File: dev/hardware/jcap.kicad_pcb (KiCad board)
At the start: 2 copper layers, 133 x 87 mm, 63 parts, among them J201 CPU PGMR, J202 SPARE CPU HDR, J203 GPU PGMR, J204 SPARE GPU HDR, J301 DC IN, J501 VGA OUT, J601 CONTROLS, SW201 CPU ~{RES}, SW202 DEBUG, SW203 GPU ~{RES}, SW601 TILT, U201 P8X32A-D40, U202 P8X32A-D40, U301 LF33_TO220, U401 24LC256, U402 24LC256, U601 74HC165, U602 74HC165, Y201 6.5MHz, Y202 6.5MHz

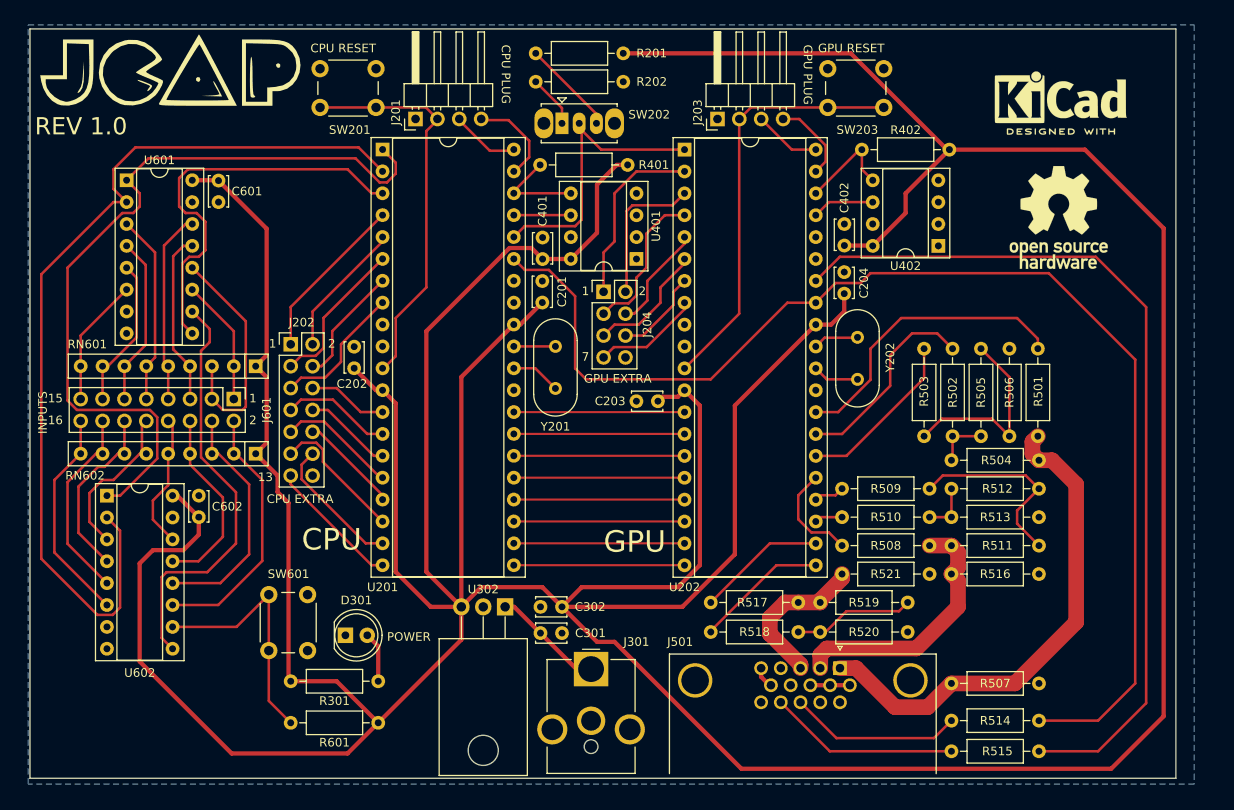
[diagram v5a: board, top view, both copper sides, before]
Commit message: Implemented review changes - missing reverse polarity protection
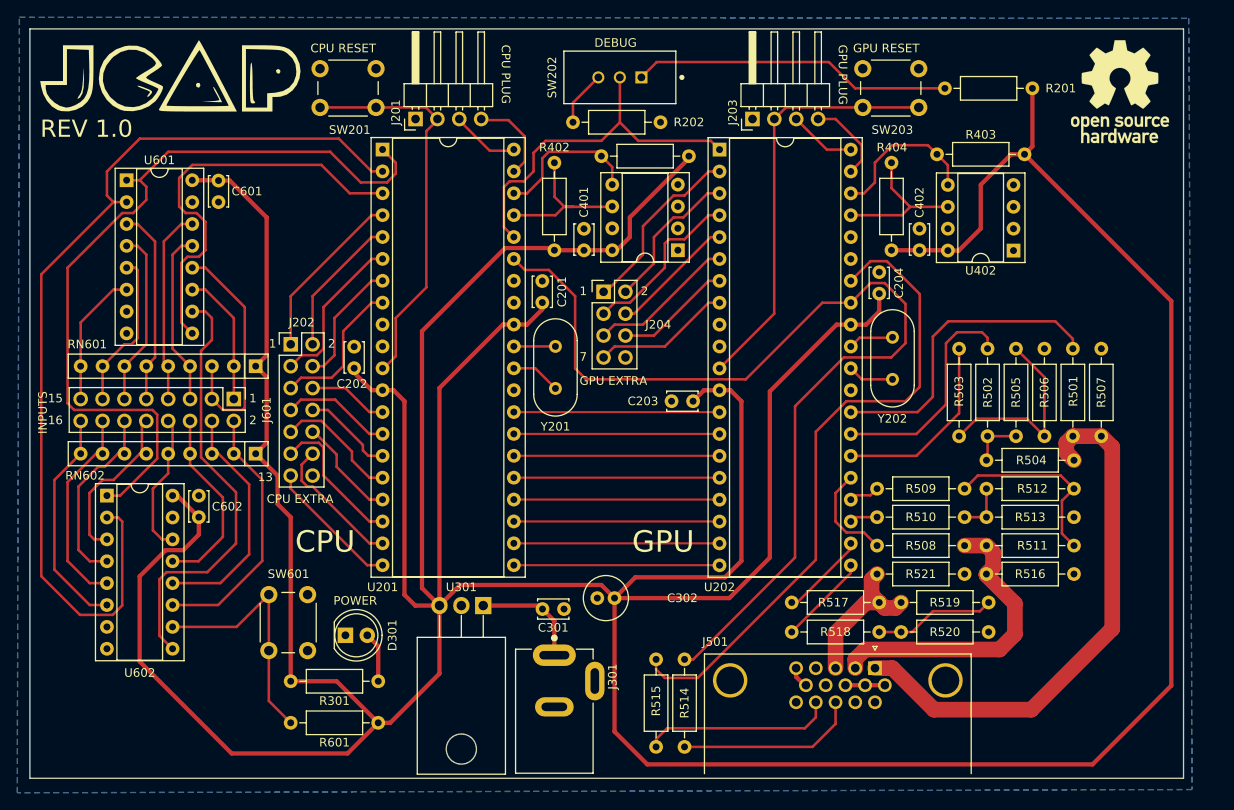
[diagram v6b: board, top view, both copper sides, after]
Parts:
- removed the REF** at (217.7, 73.9)
- added R402: 4.7K, Resistor_THT:R_Axial_DIN0207_L6.3mm_D2.5mm_P10.16mm_Horizontal, F.Cu at (158.9, 81.5)
- added R404: 4.7K, Resistor_THT:R_Axial_DIN0207_L6.3mm_D2.5mm_P10.16mm_Horizontal, F.Cu at (198.0, 81.5)
- C301: value 0.1u -> .47u
- C302: value 10u -> 47u; footprint Capacitor_THT:C_Disc_D3.4mm_W2.1mm_P2.50mm -> Capacitor_THT:C_Radial_D5.0mm_H11.0mm_P2.00mm
- G***: footprint LOGO -> jcap-footprints:LOGO
- J301: footprint Connector_BarrelJack:BarrelJack_CUI_PJ-063AH_Horizontal_CircularHoles -> jcap-footprints:CUI_PJ-202AH
- R401: value 10K -> 4.7K
- R403: renamed from R402; value 10K -> 4.7K
- SW202: footprint Button_Switch_THT:SW_Slide_1P2T_CK_OS102011MS2Q -> jcap-footprints:SW_1825159-1
- U301: footprint Package_TO_SOT_THT:TO-220-3_Horizontal_TabDown -> jcap-footprints:TO-220-3_Horizontal_TabDown
- moved R201 47.7 mm to (204.2, 72.9)
- moved R514 41.8 mm to (174.0, 139.2), turned to -90 degrees
- moved R507 39.5 mm to (222.4, 103.1), turned to -90 degrees
- moved R515 34.3 mm to (170.7, 149.4), turned to 90 degrees
- moved REF** 16.2 mm to (224.5, 73.3)
- moved R517 9.40 mm to (196.6, 132.6)
- moved R518 9.40 mm to (196.6, 136.0)
- moved R519 9.40 mm to (199.1, 132.6)
- moved R520 9.40 mm to (199.1, 136.0)
- moved C402 8.74 mm to (201.3, 89.2)
- moved R403 8.74 mm to (203.3, 80.6)
- moved U402 8.74 mm to (212.2, 91.7)
- moved C302 8.66 mm to (165.9, 132.1), turned to 180 degrees
- moved SW202 8.58 mm to (166.5, 71.6), turned to 180 degrees
- moved R401 7.18 mm to (164.3, 80.8)
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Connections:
- C302 pad 1: GND -> +3.3V
- C302 pad 2: +3.3V -> GND
- R201 pad 1: Net-(SW202-C) -> Net-(R201-Pad1)
- R202 pad 2: Net-(SW202-A) -> Net-(R202-Pad2)
- SW202 pad 1: Net-(SW202-A) -> Net-(R201-Pad1)
- SW202 pad 3: Net-(SW202-C) -> Net-(R202-Pad2)
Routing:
- net Net-(R201-Pad1): track 0.00 -> 37.2 mm
- net +3.3V: track 642.8 -> 612.8 mm
- net H_SYNC: track 102.7 -> 76.2 mm
- net V_SYNC: track 142.7 -> 117.5 mm
- net SCL_CPU: track 6.62 -> 18.3 mm
- net Net-(SW202-C): track 11.0 -> 0.00 mm
- net SCL_GPU: track 7.24 -> 17.7 mm
- net /Propellers/DEBUG: track 33.8 -> 42.2 mm
- net SDA_GPU: track 11.5 -> 18.2 mm
- net Net-(R202-Pad2): track 0.00 -> 6.43 mm
- net SDA_CPU: track 11.2 -> 17.3 mm
- net Net-(SW202-A): track 6.09 -> 0.00 mm
- net /VGA_DAC/GREEN_OUT: track 30.4 -> 35.6 mm
- net BLUE1: track 15.0 -> 10.1 mm
- net BLUE2: track 15.5 -> 10.6 mm
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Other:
- board size 133 x 87 mm -> 133.9 x 87 mm
- board text added: "DEBUG"
- board text removed: "U302"

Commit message: Finalized physical layout
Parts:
- added Q301: IPP80P03P4L-04, Package_TO_SOT_THT:TO-220-3_Horizontal_TabDown, F.Cu at (134.9, 151.0)
- moved D301 47.4 mm to (180.6, 147.8), turned to 90 degrees
- moved R301 46.3 mm to (174.5, 139.2), turned to -90 degrees
- moved J501 17.8 mm to (213.9, 140.2)
- moved R514 17.5 mm to (191.5, 139.2)
- moved R515 17.3 mm to (188.0, 149.4)
- moved R601 14.9 mm to (118.4, 135.4), turned to -90 degrees
- moved C302 13.9 mm to (179.6, 134.4)
- moved R520 12.7 mm to (186.4, 136.0)
- moved R518 12.0 mm to (206.5, 129.3)
- moved R521 9.98 mm to (199.1, 136.0), turned to 0 degrees
- moved C301 8.99 mm to (156.3, 141.5), turned to 0 degrees
- moved J301 6.57 mm to (165.4, 145.0)
- moved SW601 4.23 mm to (128.3, 135.4)
- moved U301 1.11 mm to (151.6, 132.5)
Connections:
- C301 pad 2: Net-(U301-IN) -> Net-(Q301-S)
- J301 pad 1: Net-(U301-IN) -> Net-(Q301-S)
- U301 pad 1: Net-(U301-IN) -> Net-(Q301-D)
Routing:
- net Net-(Q301-S): track 0.00 -> 33.4 mm
- net +3.3V: track 612.8 -> 581.5 mm
- net Net-(Q301-D): track 0.00 -> 26.3 mm
- net /VGA_DAC/RED_OUT: track 63.1 -> 41.2 mm
- net /VGA_DAC/GREEN_OUT: track 35.6 -> 21.1 mm
- net Net-(R518-Pad1): track 14.1 -> 27.6 mm
- net Net-(U301-IN): track 13.0 -> 0.00 mm
- net Net-(U602-DS): track 28.7 -> 15.7 mm
- net H_SYNC: track 76.2 -> 65.9 mm
- net BLUE2: track 10.6 -> 3.47 mm
- net V_SYNC: track 117.5 -> 122.8 mm
- net Net-(D301-A): track 5.86 -> 8.53 mm
- net /VGA_DAC/BLUE_OUT: track 17.6 -> 18.8 mm
- net Net-(J501-Pad14): track 22.2 -> 22.9 mm
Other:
- board text added: "+5V DC"
- board text added: "GFX_DATA[0]"
- board text added: "GFX_DATA[1]"
- board text added: "GFX_DATA[2]"
- board text added: "GFX_DATA[3]"
- board text added: "GFX_DATA[4]"
- board text added: "GFX_DATA[5]"
- board text added: "GFX_DATA[6]"
- board text added: "GFX_DATA[7]"
- board text added: "TILT"

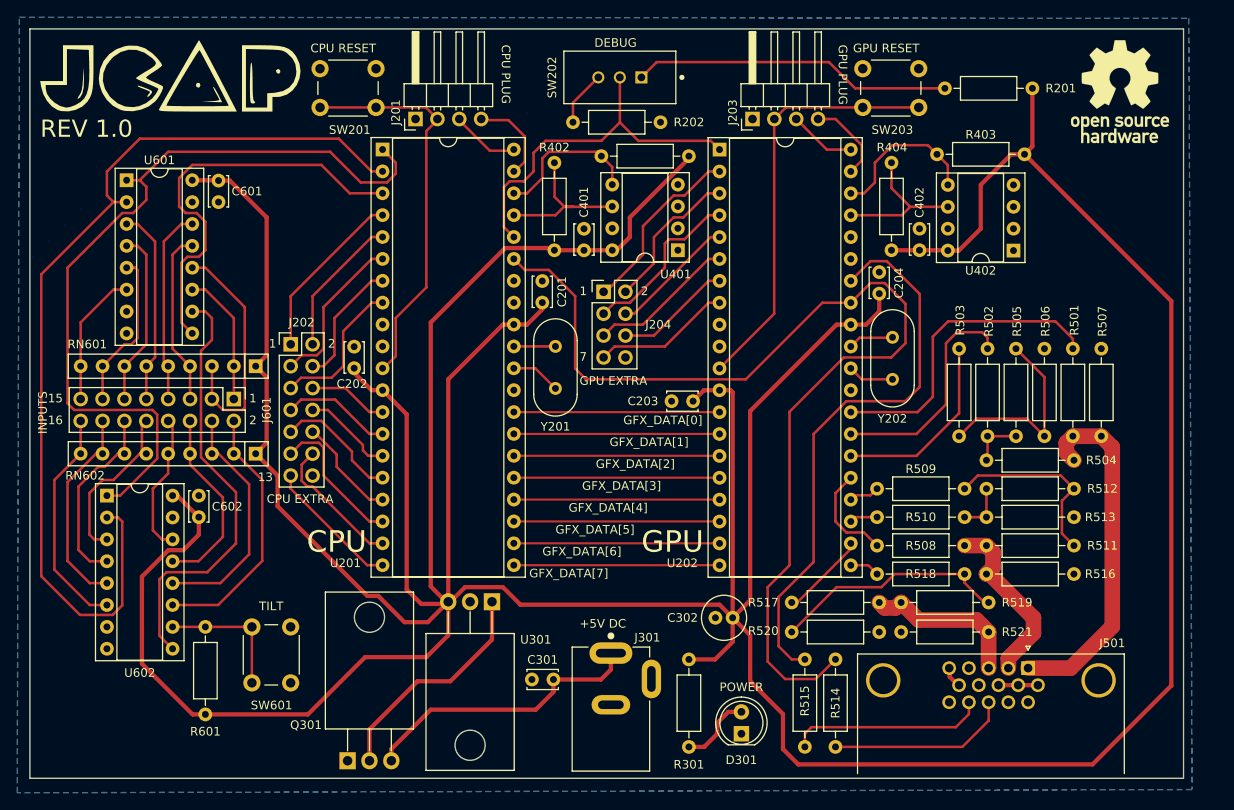
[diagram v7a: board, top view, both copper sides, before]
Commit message: Finalized dev PCB for 1st run
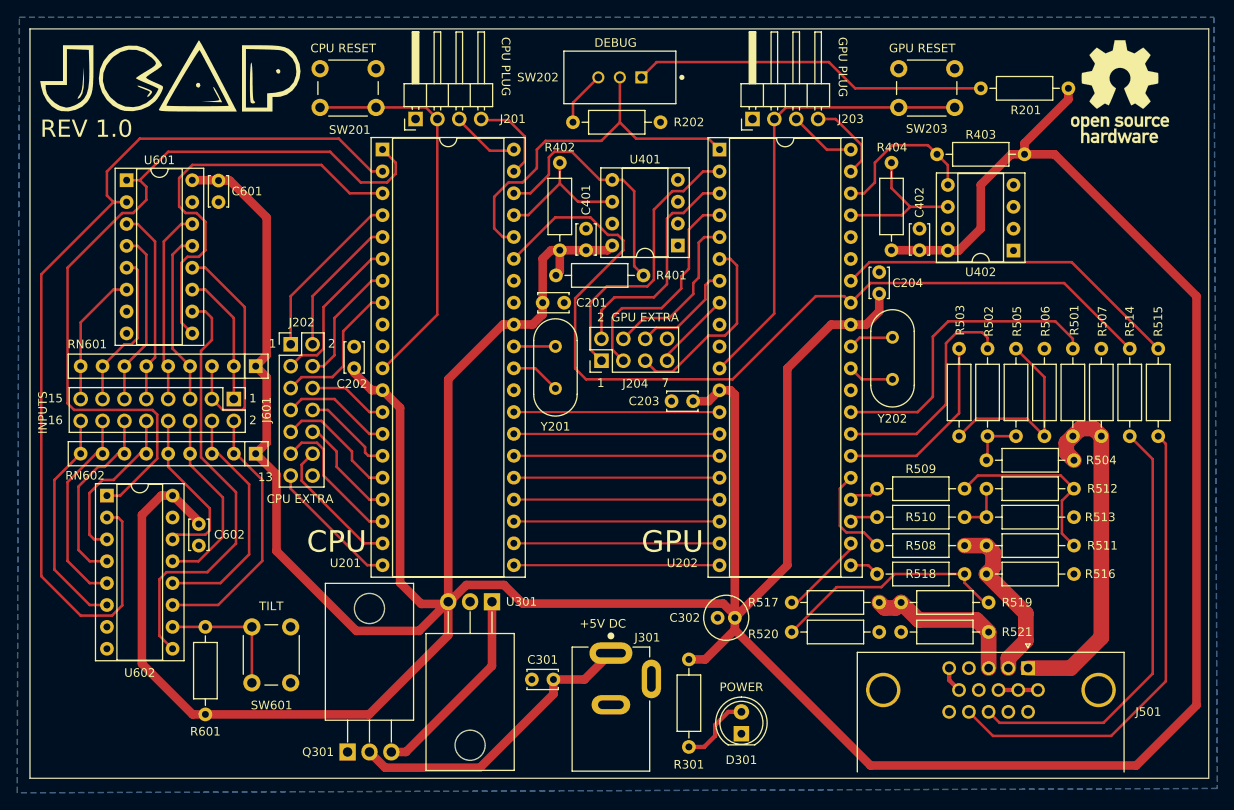
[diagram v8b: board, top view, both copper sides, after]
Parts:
- J501: footprint Connector_Dsub:DSUB-15-HD_Female_Horizontal_P2.29x1.98mm_EdgePinOffset8.35mm_Housed_MountingHolesOffset10.89mm -> jcap-footprints:2311763-2
- moved R515 54.6 mm to (229.0, 113.3)
- moved R514 49.7 mm to (225.7, 103.1)
- moved R401 14.7 mm to (169.2, 94.6), turned to 180 degrees
- moved J204 8.00 mm to (164.3, 104.5), turned to 90 degrees
- moved C602 5.80 mm to (117.6, 126.0), turned to 90 degrees
- moved SW203 4.18 mm to (198.9, 70.6)
- moved R201 4.18 mm to (208.4, 72.9)
- moved C201 3.58 mm to (160.0, 97.8), turned to 180 degrees
- moved Q301 1.02 mm to (134.9, 149.9)
- moved R402 0.63 mm to (159.5, 81.5)
- moved U401 0.55 mm to (173.2, 91.1)
- moved C302 0.25 mm to (179.8, 134.4)
- moved C401 0.24 mm to (162.6, 89.2)
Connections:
- C301 pad 2: Net-(Q301-S) -> Net-(Q301-D)
- J301 pad 1: Net-(Q301-S) -> Net-(Q301-D)
- U301 pad 1: Net-(Q301-D) -> Net-(Q301-S)
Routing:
- net +3.3V: track 581.5 -> 534.6 mm
- net Net-(J501-Pad14): track 22.9 -> 55.5 mm
- net Net-(J501-Pad13): track 21.2 -> 50.6 mm
- net H_SYNC: track 65.9 -> 40.7 mm
- net V_SYNC: track 122.8 -> 106.3 mm
- net /Propellers/GPU_SPARE_1: track 21.2 -> 33.3 mm
- net SDA_CPU: track 17.3 -> 29.3 mm
- net Net-(Q301-S): track 33.4 -> 23.3 mm
- net /Propellers/GPU_SPARE_2: track 17.4 -> 27.1 mm
- net Net-(Q301-D): track 26.3 -> 35.3 mm
- net /Propellers/GPU_SPARE_7: track 16.1 -> 9.25 mm
- net /Propellers/GPU_SPARE_3: track 19.8 -> 26.4 mm
- net /Propellers/GPU_SPARE_5: track 17.1 -> 22.6 mm
- net /Propellers/GPU_SPARE_4: track 14.6 -> 19.2 mm
- net /Propellers/~{SER_RES_GPU}: track 48.9 -> 53.1 mm
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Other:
- board size 133.9 x 87 mm -> 136.8 x 87 mm
- board text removed: "GFX_DATA[0]"
- board text removed: "GFX_DATA[1]"
- board text removed: "GFX_DATA[2]"
- board text removed: "GFX_DATA[3]"
- board text removed: "GFX_DATA[4]"
- board text removed: "GFX_DATA[5]"
- board text removed: "GFX_DATA[6]"
- board text removed: "GFX_DATA[7]"
